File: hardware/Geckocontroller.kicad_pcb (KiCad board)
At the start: 2 copper layers, 114.3 x 96.5 mm, 113 parts, among them J101 AC Input, J11 I²C (BME280), J21 RGB LED, J31 DS18B20 I, J32 DS18B20 II, J40 FAN, J51 USB-C, J60 Load Cell Connector, J70 SPI / Addon Connector, J81 Dimmer, J91 Pump, J92 HeatBed, J93 HeatLamp, K81 AQG12212, K91 AQG12112, K92 AQG12112, K93 AQG12112, Q21 AO3400A, Q22 AO3400A, Q23 AO3400A, Q40 AO3400A, Q41 AO3401A, Q51 S8050, Q52 S8050, Q61 S8550, Q81 AO3400A, Q91 AO3400A, Q92 AO3400A, Q93 AO3400A, SW1 Boot, SW2 Reset, U1 ESP32-WROOM-32, U101 ACT4088, U2 CP2102, U61 HX711, U81 6N138

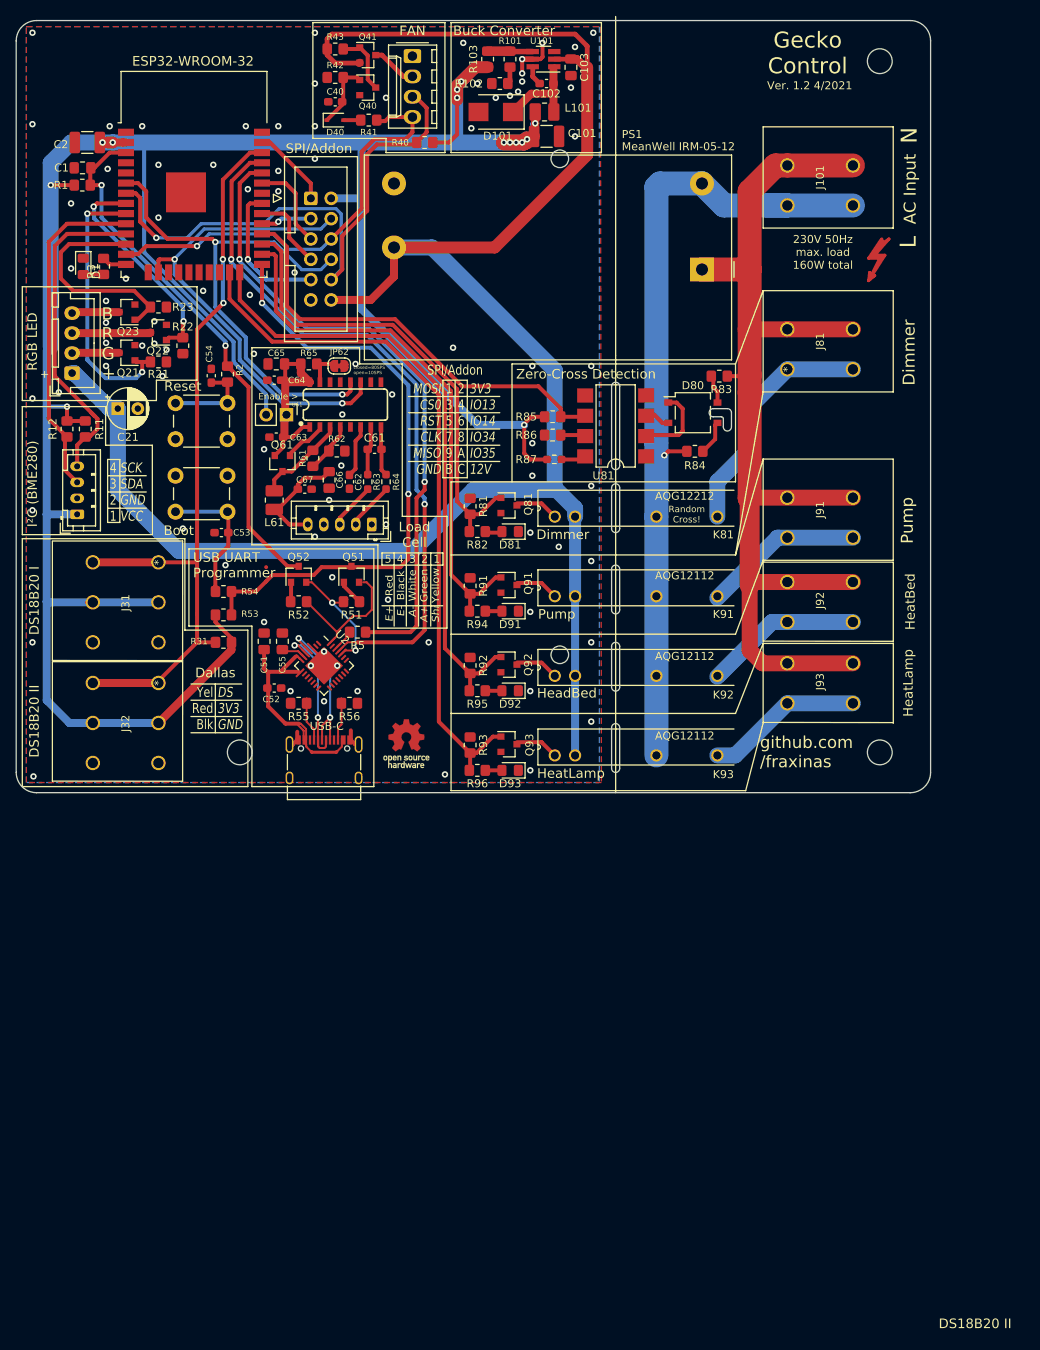
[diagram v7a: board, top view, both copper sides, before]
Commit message: hardware: wire GPIO12 to addon header, layout improvements
* add 6-pin UART header
* new, larger OSHW logo
* new, smaller solder jumper for HX711
* switch RGB-LED & I2C modules and respective part numbers
* renumber some USB programmer parts
* improve silkscreen inscriptions
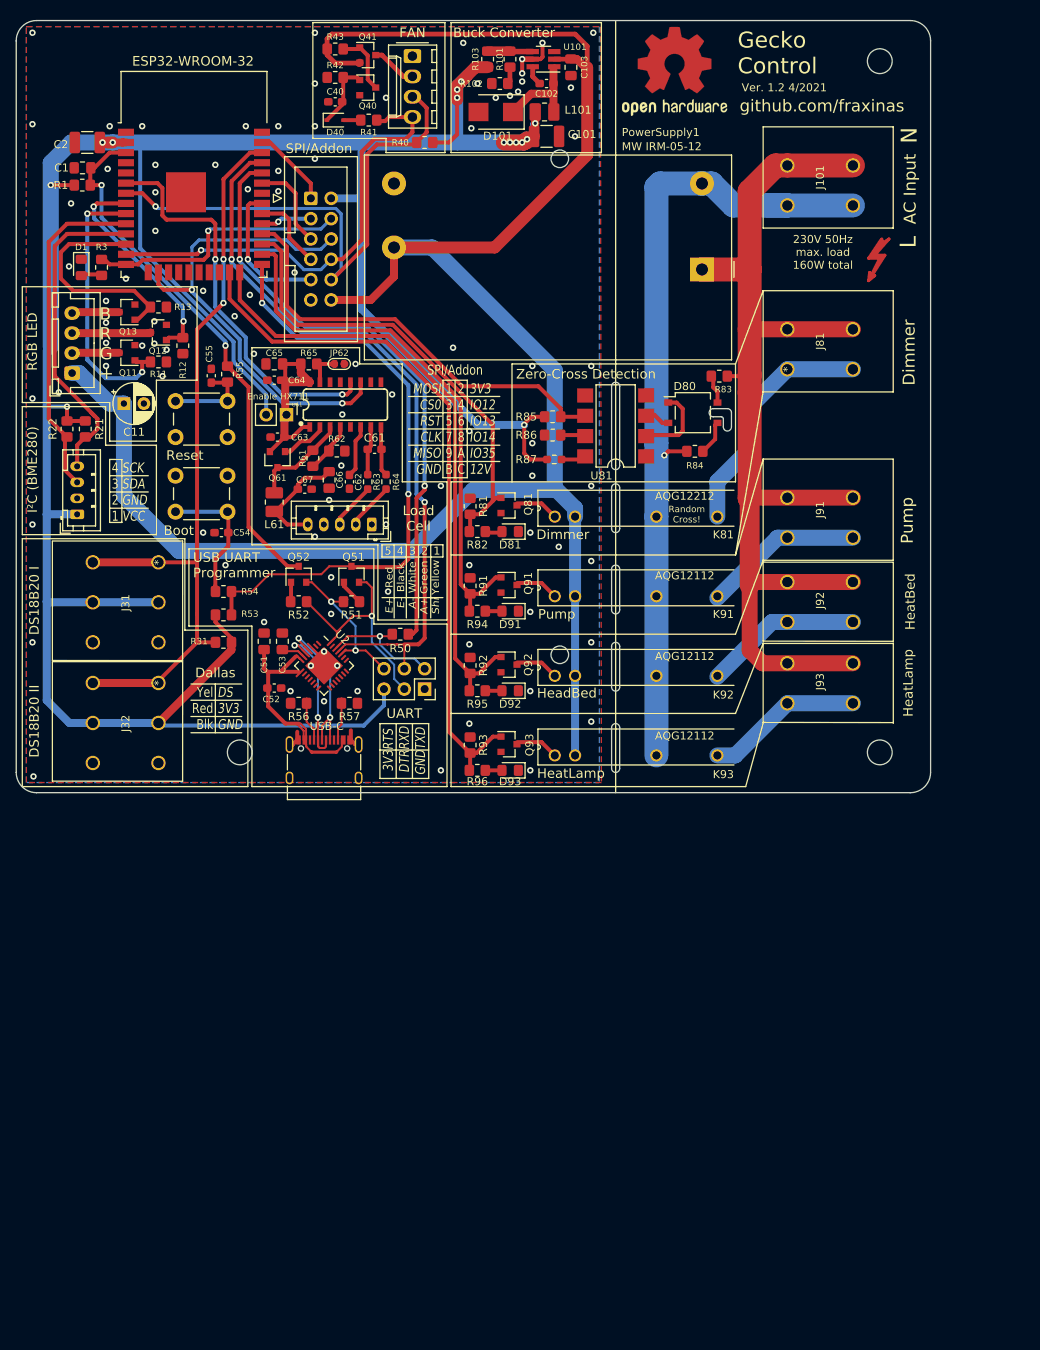
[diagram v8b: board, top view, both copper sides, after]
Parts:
- removed ?: , 
- removed the REF** at (64.0, 103.1)
- added J51: UART, Connector_PinSocket_2.54mm:PinSocket_2x03_P2.54mm_Vertical, F.Cu at (66.3, 96.3)
- added LOGO1: Logo_Open_Hardware_Small, Fraxinas:OSHW-Logo2_14.6x12mm_Mask, F.Cu at (97.5, 19.1)
- JP61: value Enable > -> Enable HX711
- JP62: footprint Jumper:SolderJumper-2_P1.3mm_Bridged_RoundedPad1.0x1.5mm -> Fraxinas:SolderJumper-2_Open_Mini
- PowerSupply1: renamed from PS1; value MeanWell IRM-05-12 -> MW IRM-05-12
- moved R50 5.34 mm to (63.2, 89.4), turned to 180 degrees
- moved C11 0.99 mm to (28.7, 60.6)
- moved Q61 0.79 mm to (47.9, 67.6)
- moved D1 0.28 mm to (23.4, 43.6)
- moved R3 0.28 mm to (25.9, 43.6)
- moved C65 0.25 mm to (47.5, 55.6)
- moved JP62 0.25 mm to (55.6, 55.6)
- moved SW2 0.25 mm to (41.7, 64.8)
- moved L61 0.25 mm to (47.5, 72.9)
- moved C63 0.15 mm to (47.9, 64.8)
- renumbered C21 to C11, C55 to C53, C53 to C54, C54 to C55, J21 to J11, J11 to J21, J51 to J50, Q21 to Q11, Q22 to Q12, Q23 to Q13, R21 to R11, R22 to R12, R23 to R13, R11 to R21, R12 to R22, R5 to R50, R2 to R55, R55 to R56, R56 to R57
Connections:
- J70 pad 4: HX_CLK -> GPIO12
- J70 pad 6: FAN_PWM -> HX_CLK
- J70 pad 8: HX_DATA -> FAN_PWM
- R3 pad 1: Net-(R3-Pad1) -> GPIO12
- R50 pad 1: RXD0' -> RXD0
- R50 pad 2: Net-(R5-Pad2) -> /TXD
- U1 pad 14: Net-(R3-Pad1) -> GPIO12
- U1 pad 34: Net-(R5-Pad2) -> RXD0
- U2 pad 26: RXD0' -> /TXD
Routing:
- net Net-(R5-Pad2): track 79.6 -> 0.00 mm, vias 2 -> 0
- net RXD0: track 0.00 -> 74.9 mm, vias 0 -> 2
- net GPIO12: track 0.00 -> 33.5 mm, vias 0 -> 1
- net +3V3: track 329.1 -> 361.0 mm
- net HX_DATA: track 65.6 -> 49.9 mm
- net /TXD: track 0.00 -> 15.4 mm, vias 0 -> 1
- net /DTR: track 16.8 -> 28.6 mm, vias 0 -> 1
- net FAN_SIG: track 73.1 -> 68.3 mm
- net /RTS: track 15.6 -> 20.3 mm
- net TXD0: track 87.5 -> 91.1 mm
- net FAN_PWM: track 54.9 -> 58.4 mm
- net Net-(R3-Pad1): track 3.11 -> 0.00 mm
- net RXD0': track 2.66 -> 0.00 mm
- net /AVDD: track 11.5 -> 12.4 mm
- net +12V: track 254.0 -> 254.8 mm
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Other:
- board text added: "3V3 DTR GND"
- board text added: "3V3 IO12 IO13 IO14 IO35 12V"
- board text added: "RTS RXD TXD"
- board text added: "github.com/fraxinas"
- board text removed: "+"
- board text removed: "3V3 IO13 IO14 IO34 IO35 12V"
- board text removed: "github.com /fraxinas"
